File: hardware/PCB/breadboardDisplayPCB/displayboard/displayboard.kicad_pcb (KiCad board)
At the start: 2 copper layers, 306 x 49.8 mm, 49 parts, among them J1 Conn_01x09_Socket, Q1 2N7000, U1 74HC595, U2 74HC595, U3 74HC595, U4 74HC595, U5 74HC595, U6 TBD62783A, U7 TBD62783A, U8 ULN2803A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

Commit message: begin work on final display PCB
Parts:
- removed MH1, MH2, MH3: MountingHole_3.2mm_M3, MountingHole:MountingHole_3.2mm_M3
- added C6: 100nF, Capacitor_SMD:C_0603_1608Metric, B.Cu at (410.6, 144.2)
- added LED1: WP113IDT, SamacSys_Parts:WP113IDT, F.Cu at (283.5, 111.0)
- added LED2: WP113IDT, SamacSys_Parts:WP113IDT, F.Cu at (291.0, 111.0)
- added LED3: WP113IDT, SamacSys_Parts:WP113IDT, F.Cu at (298.5, 111.0)
- added Q2: TEPT5700, SamacSys_Parts:TEPT5700, F.Cu at (469.2, 112.0)
- added R18: 10k, Resistor_SMD:R_0805_2012Metric, B.Cu at (381.1, 156.7)
- added R19: 1k, Resistor_SMD:R_0603_1608Metric, B.Cu at (375.6, 131.1)
- added R20: 1k, Resistor_SMD:R_0603_1608Metric, B.Cu at (421.4, 131.2)
- added R21: 1k, Resistor_SMD:R_0603_1608Metric, B.Cu at (401.1, 126.2)
- added REF**: MountingHole_3.2mm_M3_Pad_Via, MountingHole:MountingHole_3.2mm_M3_Pad_Via, F.Cu at (275.5, 112.2)
- added REF**: MountingHole_3.2mm_M3_Pad_Via, MountingHole:MountingHole_3.2mm_M3_Pad_Via, F.Cu at (488.5, 112.2)
- added REF**: MountingHole_3.2mm_M3_Pad_Via, MountingHole:MountingHole_3.2mm_M3_Pad_Via, F.Cu at (488.5, 81.8)
- added REF**: MountingHole_3.2mm_M3_Pad_Via, MountingHole:MountingHole_3.2mm_M3_Pad_Via, F.Cu at (275.5, 81.8)
- C1, C2, C3, C4, C5: footprint Capacitor_THT:C_Disc_D5.0mm_W2.5mm_P5.00mm -> Capacitor_SMD:C_0603_1608Metric; moved to B.Cu
- J1: footprint Connector_PinHeader_2.54mm:PinHeader_1x09_P2.54mm_Vertical -> Connector_JST:JST_XH_B9B-XH-A_1x09_P2.50mm_Vertical; moved to B.Cu
- Q1: value 2N7000 -> 2N7002; footprint Package_TO_SOT_THT:TO-92_Inline -> Package_TO_SOT_SMD:SOT-23; moved to B.Cu
- R1, R10, R11, R12, R13, R14, R15, R16, R17, R2, R3, R4, R5, R6, R7, R8, R9: footprint Resistor_THT:R_Axial_DIN0207_L6.3mm_D2.5mm_P7.62mm_Horizontal -> Resistor_SMD:R_0805_2012Metric; moved to B.Cu
- R101: footprint Resistor_THT:R_Axial_DIN0207_L6.3mm_D2.5mm_P7.62mm_Horizontal -> Resistor_SMD:R_0603_1608Metric; moved to B.Cu
- U1, U2, U3, U4, U5: footprint Package_DIP:DIP-16_W7.62mm_Socket -> Package_SO:SOIC-16_3.9x9.9mm_P1.27mm; moved to B.Cu
- U6, U7, U8, U9: footprint Package_DIP:DIP-18_W7.62mm_Socket -> Package_SO:SOIC-18W_7.5x11.6mm_P1.27mm; moved to B.Cu
- moved U1 201.3 mm to (475.6, 81.2), turned to -90 degrees
- moved U3 193.8 mm to (431.2, 112.2), turned to -90 degrees
- moved U2 186.7 mm to (441.6, 81.2), turned to -90 degrees
- moved U9 177.8 mm to (450.0, 100.2), turned to 0 degrees
- moved C3 174.2 mm to (413.1, 126.2), turned to 180 degrees
- moved U8 173.1 mm to (466.9, 100.2), turned to 180 degrees
- moved R7 160.5 mm to (462.0, 110.7), turned to -90 degrees
- moved Q1 159.5 mm to (415.0, 111.7), turned to 90 degrees
- moved U7 158.1 mm to (381.9, 101.0), turned to 180 degrees
- moved R6 157.4 mm to (460.0, 110.7), turned to -90 degrees
- moved C2 154.7 mm to (433.4, 131.2), turned to 180 degrees
- moved R5 154.3 mm to (458.0, 110.7), turned to -90 degrees
- moved R4 151.3 mm to (456.0, 110.7), turned to -90 degrees
- moved R3 148.3 mm to (454.0, 110.7), turned to -90 degrees
- moved J1 146.6 mm to (369.5, 112.0), turned to 180 degrees
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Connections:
- J1 pad 9: /GND -> /ANALOG
- LED_ALPHA10 pad 18: /ANODE10_5V -> /ANODE1_5V
- LED_ALPHA11 pad 18: /ANODE11_5V -> /ANODE1_5V
- LED_ALPHA12 pad 18: /ANODE12_5V -> /ANODE1_5V
- LED_ALPHA2 pad 18: /ANODE2_5V -> /ANODE1_5V
- LED_ALPHA3 pad 18: /ANODE3_5V -> /ANODE1_5V
- LED_ALPHA4 pad 18: /ANODE4_5V -> /ANODE1_5V
- LED_ALPHA5 pad 18: /ANODE5_5V -> /ANODE1_5V
- LED_ALPHA6 pad 18: /ANODE6_5V -> /ANODE1_5V
- LED_ALPHA7 pad 18: /ANODE7_5V -> /ANODE1_5V
- LED_ALPHA8 pad 18: /ANODE8_5V -> /ANODE1_5V
- LED_ALPHA9 pad 18: /ANODE9_5V -> /ANODE1_5V
- Q1 pad 1: Net-(Q1-S) -> /SEG_DPpretransistor
- Q1 pad 2: /SEG_DPpretransistor -> Net-(Q1-S)
- U5 pad 5: unconnected-(U5-QF-Pad5) -> /LED1
- U5 pad 6: unconnected-(U5-QG-Pad6) -> /LED2
- U5 pad 7: unconnected-(U5-QH-Pad7) -> /LED3
- U7 pad 1: unconnected-(U7-I1-Pad1) -> /LED3
- U7 pad 16: unconnected-(U7-O3-Pad16) -> /LED1_5V
- U7 pad 17: unconnected-(U7-O2-Pad17) -> /LED2_5V
- U7 pad 18: unconnected-(U7-O1-Pad18) -> /LED3_5V
- U7 pad 2: unconnected-(U7-I2-Pad2) -> /LED2
- U7 pad 3: unconnected-(U7-I3-Pad3) -> /LED1
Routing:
- net /3v3: track 478.6 -> 0.00 mm, vias 5 -> 0
- net /SRCLK: track 449.9 -> 0.00 mm, vias 4 -> 0
- net /OE_PWM: track 394.1 -> 0.00 mm, vias 3 -> 0
- net /RCLK: track 374.3 -> 0.00 mm, vias 4 -> 0
- net /5v: track 347.0 -> 0.00 mm, vias 3 -> 0
- net /SEG_N: track 246.2 -> 0.00 mm, vias 1 -> 0
- net /SEG_P: track 242.2 -> 0.00 mm, vias 1 -> 0
- net /SEG_M: track 241.8 -> 0.00 mm
- net /SEG_U: track 239.1 -> 0.00 mm
- net /SEG_K: track 237.6 -> 0.00 mm, vias 1 -> 0
- net /SEG_R: track 234.8 -> 0.00 mm, vias 1 -> 0
- net /SEG_S: track 230.7 -> 0.00 mm, vias 1 -> 0
- net /SEG_T: track 228.1 -> 0.00 mm
- net /SEG_DP: track 220.5 -> 0.00 mm
- net /SEG_D: track 218.5 -> 0.00 mm
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- removed copper zone on B.Cu, net /GND
- removed copper zone on F.Cu, net /GND
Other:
- board size 306 x 49.8 mm -> 223 x 45.3 mm
- board text removed: "12C-LTP-587HR"
- board text removed: "2026-01-06"
- board text removed: "3v3"
- board text removed: "5v"
- board text removed: "DECIMAL POINT TRANSISTOR"
- board text removed: "GND"
- board text removed: "HAPPY NEW YEAR"
- board text removed: "HELLO FROM CINCINNATI :)"
- board text removed: "MOUNTING HOLES M3 SCREWS 20mm SPACING"
- board text removed: "NATHANIEL KESSEL"
- board text removed: "NATHANIEL KESSEL DRIVERS AND DIGITS FOR BREADBOARD DESIGNED FOR LITE-ON LTP-587HR SEGMENTED DISPLAY REVISION C 2026-01-06 DESIGNED IN KICAD"
- board text removed: "OE_PWM"
- board text removed: "RCLK"
- board text removed: "REV C"
- board text removed: "SERIAL"
- board text removed: "SRCLK"
- board text removed: "STITCHING"
- board text removed: "|||||||||||||||||||| |||||| |||||||||||||||||| ||||||||"

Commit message: final PCB rev work
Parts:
- moved R20 111.0 mm to (312.4, 110.2), turned to 90 degrees
- moved R18 108.5 mm to (482.5, 118.1), turned to 90 degrees
- moved R21 91.7 mm to (310.8, 110.2), turned to 90 degrees
- moved C1 88.4 mm to (472.5, 106.4), turned to 90 degrees
- moved C6 72.3 mm to (478.0, 117.9), turned to 90 degrees
- moved R10 65.4 mm to (424.0, 104.1), turned to 90 degrees
- moved R19 65.0 mm to (314.0, 110.2), turned to 90 degrees
- moved R9 61.3 mm to (426.0, 104.1), turned to 90 degrees
- moved R14 56.5 mm to (407.0, 104.2), turned to 90 degrees
- moved R11 50.3 mm to (422.0, 104.1), turned to 90 degrees
- moved C5 49.7 mm to (370.7, 109.0)
- moved R8 45.4 mm to (428.0, 104.1), turned to 90 degrees
- moved C4 44.6 mm to (403.5, 109.7)
- moved R16 40.1 mm to (405.0, 104.2), turned to 90 degrees
- moved R17 38.5 mm to (409.0, 112.2), turned to 90 degrees
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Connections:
- LED_ALPHA10 pad 18: /ANODE1_5V -> /ANODE10_5V
- LED_ALPHA11 pad 18: /ANODE1_5V -> /ANODE11_5V
- LED_ALPHA12 pad 18: /ANODE1_5V -> /ANODE12_5V
- LED_ALPHA2 pad 18: /ANODE1_5V -> /ANODE2_5V
- LED_ALPHA3 pad 18: /ANODE1_5V -> /ANODE3_5V
- LED_ALPHA4 pad 18: /ANODE1_5V -> /ANODE4_5V
- LED_ALPHA5 pad 18: /ANODE1_5V -> /ANODE5_5V
- LED_ALPHA6 pad 18: /ANODE1_5V -> /ANODE6_5V
- LED_ALPHA7 pad 18: /ANODE1_5V -> /ANODE7_5V
- LED_ALPHA8 pad 18: /ANODE1_5V -> /ANODE8_5V
- LED_ALPHA9 pad 18: /ANODE1_5V -> /ANODE9_5V
- Q1 pad 2: Net-(Q1-S) -> /GND
- U3 pad 9: Net-(Q1-S) -> Net-(U3-QH')
- U4 pad 14: Net-(Q1-S) -> Net-(U3-QH')
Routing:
- net /3v3: track 0.00 -> 239.1 mm, vias 0 -> 6
- net /ANALOG: track 0.00 -> 237.0 mm
- net /SER: track 0.00 -> 233.0 mm, vias 0 -> 4
- net /ANODE9_5V: track 0.00 -> 221.7 mm, vias 0 -> 4
- net /SEG_B: track 0.00 -> 219.6 mm
- net /SEG_A: track 0.00 -> 215.9 mm
- net /SEG_N: track 0.00 -> 214.6 mm
- net /SEG_M: track 0.00 -> 214.1 mm
- net /SEG_C: track 0.00 -> 212.8 mm
- net /SEG_H: track 0.00 -> 212.3 mm
- net /SEG_P: track 0.00 -> 212.3 mm
- net /SEG_DP: track 0.00 -> 211.1 mm
- net /SEG_G: track 0.00 -> 210.8 mm
- net /SEG_K: track 0.00 -> 210.5 mm
- net /SEG_U: track 0.00 -> 208.9 mm
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- added copper zone on B.Cu, net /GND
- added copper zone on F.Cu, net /GND
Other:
- board text added: "12C-LTP-587HR"
- board text added: "NATHANIEL KESSEL"

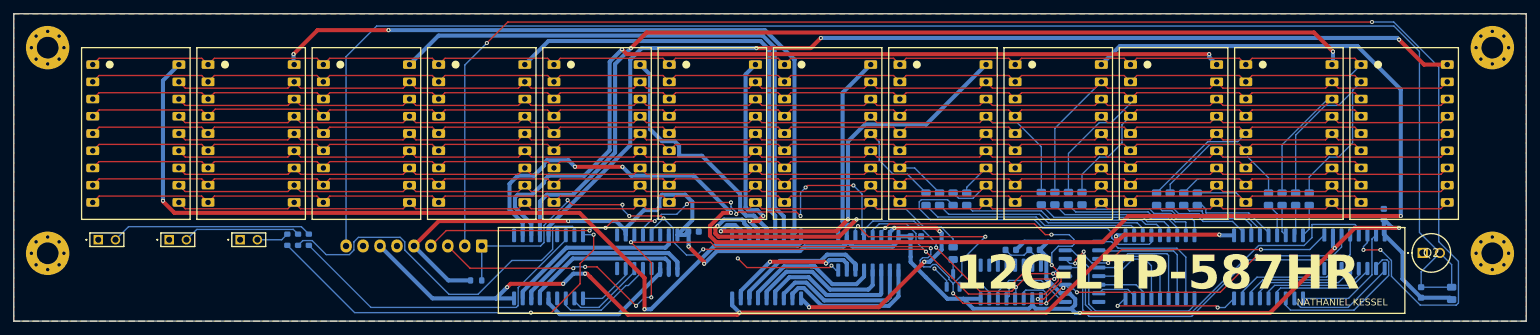
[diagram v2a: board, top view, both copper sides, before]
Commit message: rev 4 PCB design finalized for display
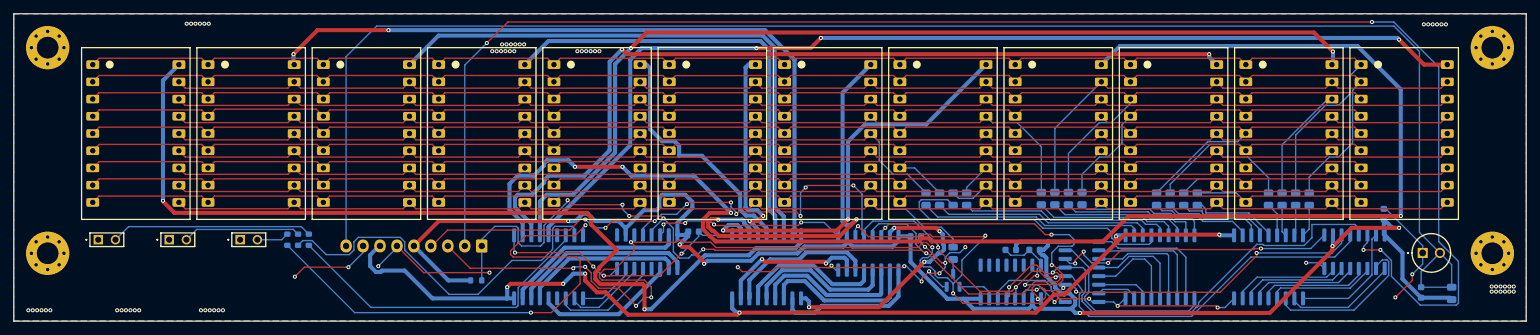
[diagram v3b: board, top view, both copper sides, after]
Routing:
- net /GND: track 45.8 -> 189.4 mm, vias 5 -> 86
- net Net-(U4-QH'): track 0.00 -> 29.0 mm, vias 0 -> 4
- net /LED3_5V: track 58.7 -> 77.9 mm
- net /SRCLK: track 201.2 -> 211.1 mm
- net /OE_PWM: track 187.8 -> 195.5 mm
- net /ANODE1_5V: track 129.6 -> 136.5 mm
- net /5v: track 145.8 -> 149.9 mm
- net /RCLK: track 171.2 -> 174.1 mm
- net /ANODE9_5V: track 221.7 -> 224.0 mm
- net /ANODE7_5V: track 57.6 -> 59.6 mm
- net /ANODE8: track 20.0 -> 21.8 mm
- net Net-(U3-QH'): track 44.9 -> 46.6 mm
- net /ANODE10: track 28.1 -> 26.7 mm
- net /ANODE11: track 24.9 -> 23.5 mm
- net /ANODE12: track 22.0 -> 20.6 mm
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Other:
- board text added: "2026-02-16"
- board text added: "3V3"
- board text added: "5V"
- board text added: "ANALOG"
- board text added: "BASED ON PRIOR 12C-LTP-587HR PCB"
- board text added: "ESPCLK-12C-DISP"
- board text added: "FOR LITE-ON LTP-587HR"
- board text added: "FOR NATHANIEL KESSEL'S ESP32 CLOCK"
- board text added: "GND"
- board text added: "HELLO FROM CINCINNATI : )"
- board text added: "KICAD 9.0"
- board text added: "NATHANIEL KESSEL REV 1"
- board text added: "OE_PWM"
- board text added: "RCLK"
- board text added: "SER"
- board text added: "SRCLK"
- board text removed: "12C-LTP-587HR"
- board text removed: "NATHANIEL KESSEL"

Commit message: large commit of PCB progress
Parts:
- added C7: 47uF, Capacitor_SMD:CP_Elec_6.3x5.4, B.Cu at (311.2, 117.8)
- U8, U9: value ULN2803A -> TBD62083A
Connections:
- net /5v renamed +5V
- net /ANALOG renamed ANALOG
- net /ANODE1_5V renamed ANODE1_5V
- net /ANODE2_5V renamed ANODE2_5V
- net /ANODE3_5V renamed ANODE3_5V
- net /ANODE4_5V renamed ANODE4_5V
- net /ANODE5_5V renamed ANODE5_5V
- net /ANODE6_5V renamed ANODE6_5V
- net /ANODE7_5V renamed ANODE7_5V
- net /ANODE8_5V renamed ANODE8_5V
- net /OE_PWM renamed OE_PWM
- net /RCLK renamed RCLK
- net /SEG_A renamed SEG_A
- net /SEG_B renamed SEG_B
- net /SEG_C renamed SEG_C
- net /SEG_D renamed SEG_D
- net /SEG_DP renamed SEG_DP
- net /SEG_E renamed SEG_E
- net /SEG_F renamed SEG_F
- net /SEG_G renamed SEG_G
- net /SEG_H renamed SEG_H
- net /SEG_K renamed SEG_K
- net /SEG_M renamed SEG_M
- net /SEG_N renamed SEG_N
- net /SEG_P renamed SEG_P
- net /SEG_R renamed SEG_R
- net /SEG_S renamed SEG_S
- net /SEG_T renamed SEG_T
- net /SEG_U renamed SEG_U
- net /SER renamed SER
- net /SRCLK renamed SRCLK
- net Net-(U3-QH') renamed ANODE_SER
- C1 pad 1: /3v3 -> +3V3
- C1 pad 2: /GND -> GND
- C2 pad 1: /3v3 -> GND
- C2 pad 2: /GND -> +3V3
- C3 pad 1: /3v3 -> GND
- C3 pad 2: /GND -> +3V3
- C4 pad 1: /GND -> +3V3
- C4 pad 2: /3v3 -> GND
- C5 pad 1: /GND -> +3V3
- C5 pad 2: /3v3 -> GND
- C6 pad 1: /3v3 -> +3V3
- J1 pad 5: /3v3 -> +3V3
- J1 pad 6: /GND -> GND
- J1 pad 8: /GND -> GND
- LED1 pad 1: /GND -> GND
- LED2 pad 1: /GND -> GND
- LED3 pad 1: /GND -> GND
- LED_ALPHA10 pad 18: /ANODE10_5V -> ANODE10_5V
- LED_ALPHA11 pad 18: /ANODE11_5V -> ANODE11_5V
- LED_ALPHA12 pad 18: /ANODE12_5V -> ANODE12_5V
- LED_ALPHA9 pad 18: /ANODE9_5V -> ANODE9_5V
- Q1 pad 2: /GND -> GND
- Q2 pad 1: /GND -> GND
- R101 pad 1: /3v3 -> +3V3
- R18 pad 1: /3v3 -> +3V3
- R19 pad 1: /LED1_5V -> LED1_5V
- R20 pad 1: /LED2_5V -> LED2_5V
- R21 pad 1: /LED3_5V -> LED3_5V
- U1 pad 10: /3v3 -> +3V3
- U1 pad 16: /3v3 -> +3V3
- U1 pad 8: /GND -> GND
- U2 pad 10: /3v3 -> +3V3
- U2 pad 16: /3v3 -> +3V3
- U2 pad 8: /GND -> GND
- U3 pad 10: /3v3 -> +3V3
- U3 pad 16: /3v3 -> +3V3
- U3 pad 8: /GND -> GND
- U4 pad 10: /3v3 -> +3V3
- U4 pad 16: /3v3 -> +3V3
- U4 pad 8: /GND -> GND
- U5 pad 10: /3v3 -> +3V3
- U5 pad 16: /3v3 -> +3V3
- U5 pad 8: /GND -> GND
- U6 pad 10: /GND -> GND
- U7 pad 1: /LED3 -> /ANODE9
- U7 pad 10: /GND -> GND
- U7 pad 11: /ANODE9_5V -> LED3_5V
- U7 pad 12: /ANODE10_5V -> LED2_5V
- U7 pad 13: /ANODE11_5V -> LED1_5V
- U7 pad 14: /ANODE12_5V -> unconnected-(U7-O5-Pad14)
- U7 pad 15: unconnected-(U7-O4-Pad15) -> ANODE12_5V
- U7 pad 16: /LED1_5V -> ANODE11_5V
- U7 pad 17: /LED2_5V -> ANODE10_5V
- U7 pad 18: /LED3_5V -> ANODE9_5V
- U7 pad 2: /LED2 -> /ANODE10
- U7 pad 3: /LED1 -> /ANODE11
- U7 pad 4: unconnected-(U7-I4-Pad4) -> /ANODE12
- U7 pad 5: /ANODE12 -> unconnected-(U7-I5-Pad5)
- U7 pad 6: /ANODE11 -> /LED1
- U7 pad 7: /ANODE10 -> /LED2
- U7 pad 8: /ANODE9 -> /LED3
- U8 pad 9: /GND -> GND
- U9 pad 9: /GND -> GND
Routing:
- net +3V3: track 0.00 -> 244.9 mm, vias 0 -> 9
- net /3v3: track 239.3 -> 0.00 mm, vias 6 -> 0
- net /ANODE9_5V: track 224.0 -> 0.00 mm, vias 4 -> 0
- net ANODE9_5V: track 0.00 -> 211.9 mm, vias 0 -> 4
- net /GND: track 189.4 -> 0.00 mm, vias 86 -> 0
- net GND: track 0.00 -> 179.8 mm, vias 0 -> 84
- net /ANODE12_5V: track 154.3 -> 0.00 mm, vias 3 -> 0
- net ANODE12_5V: track 0.00 -> 153.8 mm, vias 0 -> 3
- net /ANODE11_5V: track 142.8 -> 0.00 mm, vias 2 -> 0
- net ANODE11_5V: track 0.00 -> 139.4 mm, vias 0 -> 4
- net /ANODE10_5V: track 128.1 -> 0.00 mm, vias 2 -> 0
- net ANODE10_5V: track 0.00 -> 126.2 mm, vias 0 -> 6
- net /LED3_5V: track 77.9 -> 0.00 mm, vias 2 -> 0
- net LED3_5V: track 0.00 -> 73.4 mm, vias 0 -> 2
- net /LED2_5V: track 54.9 -> 0.00 mm
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- added copper zone on B.Cu, net GND
- added copper zone on F.Cu, net GND
- removed copper zone on B.Cu, net /GND
- removed copper zone on F.Cu, net /GND
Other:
- board text added: "NATHANIEL KESSEL REV A"
- board text removed: "NATHANIEL KESSEL REV 1"
